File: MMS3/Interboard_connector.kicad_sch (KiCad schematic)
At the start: 1 part, among them J1 86093488324755V1LF

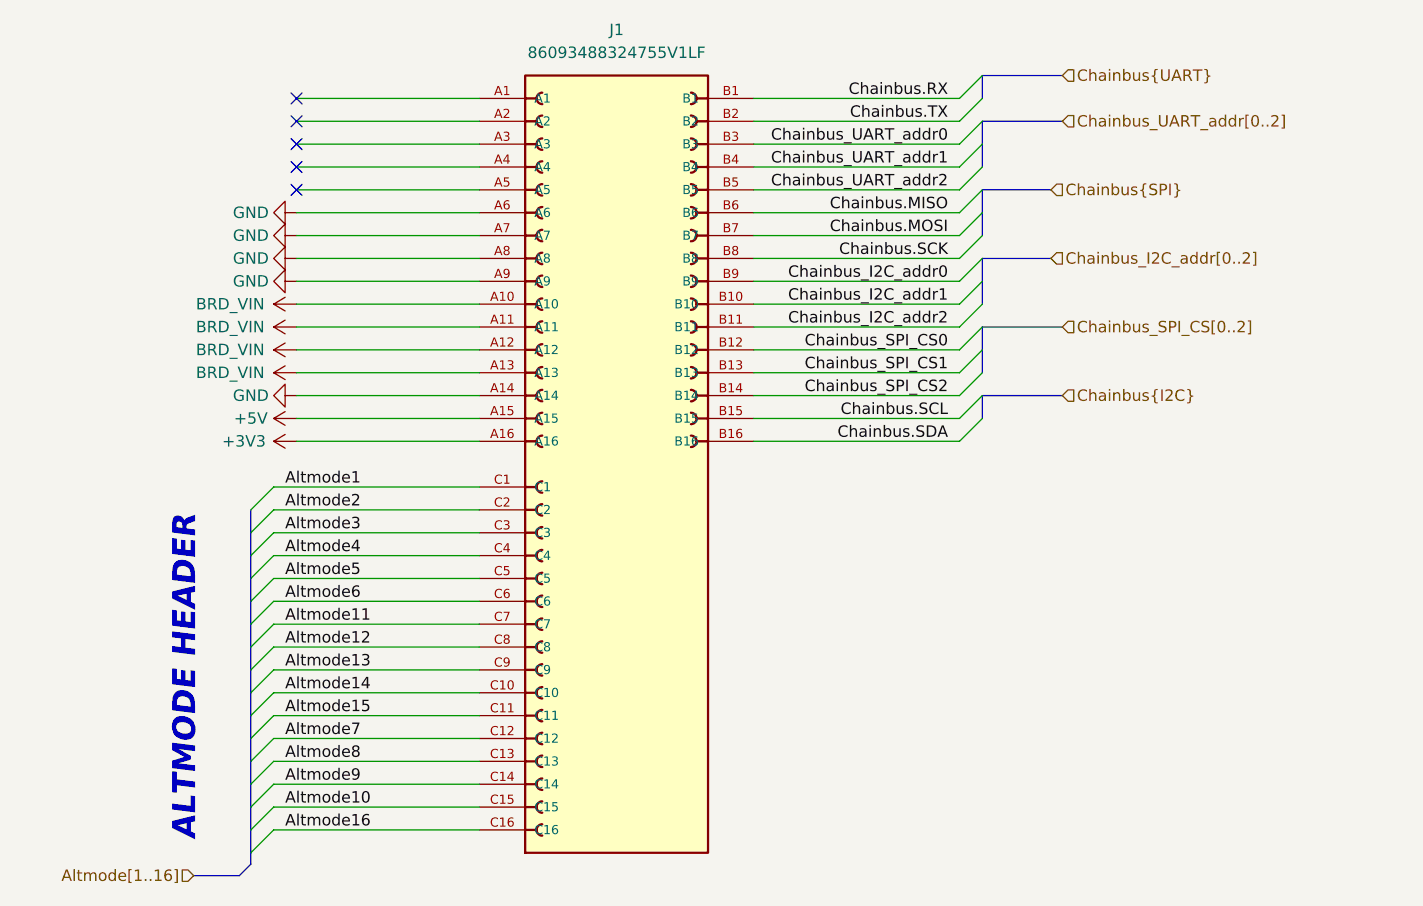
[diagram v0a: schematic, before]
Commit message: schematic + partly layout
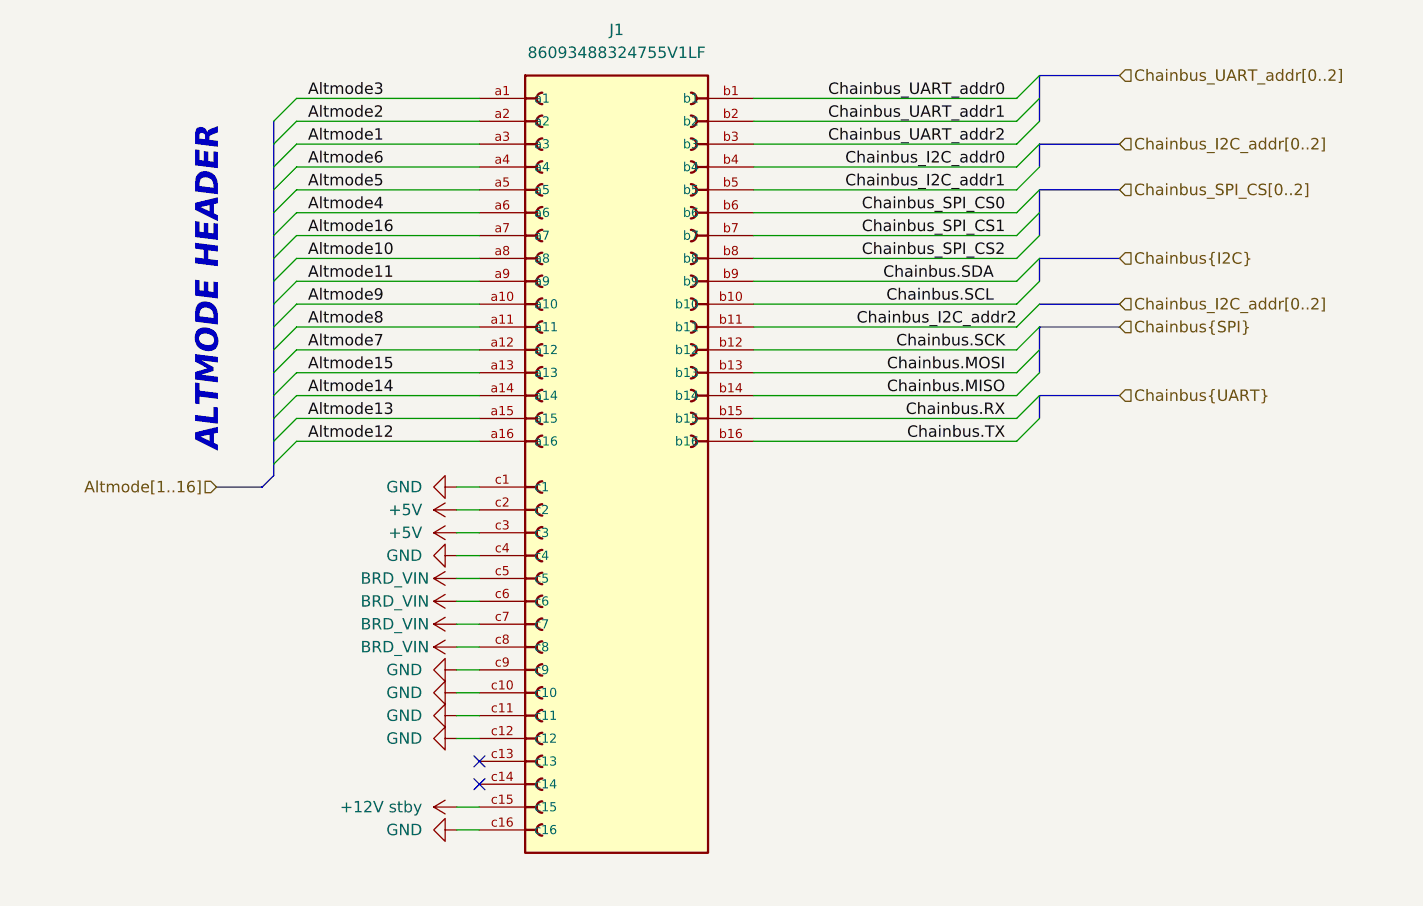
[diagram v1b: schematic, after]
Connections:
- net +5V: now also J1.c2, J1.c3; no longer J1.A15
- net Altmode1: now also J1.a3; no longer J1.C1
- net Altmode10: now also J1.a8; no longer J1.C15
- net Altmode11: now also J1.a9; no longer J1.C7
- net Altmode12: now also J1.a16; no longer J1.C8
- net Altmode13: now also J1.a15; no longer J1.C9
- net Altmode14: now also J1.a14; no longer J1.C10
- net Altmode15: now also J1.a13; no longer J1.C11
- net Altmode16: now also J1.a7; no longer J1.C16
- net Altmode2: now also J1.a2; no longer J1.C2
- net Altmode3: now also J1.a1; no longer J1.C3
- net Altmode4: now also J1.a6; no longer J1.C4
- net Altmode5: now also J1.a5; no longer J1.C5
- net Altmode6: now also J1.a4; no longer J1.C6
- net Altmode7: now also J1.a12; no longer J1.C12
- net Altmode8: now also J1.a11; no longer J1.C13
- net Altmode9: now also J1.a10; no longer J1.C14
- net BRD_VIN: now also J1.c5, J1.c6, J1.c7, J1.c8; no longer J1.A10, J1.A11, J1.A12, J1.A13
- net Chainbus.MISO: now also J1.b14; no longer J1.B6
- net Chainbus.MOSI: now also J1.b13; no longer J1.B7
- net Chainbus.RX: now also J1.b15; no longer J1.B1
- net Chainbus.SCK: now also J1.b12; no longer J1.B8
- net Chainbus.SCL: now also J1.b10; no longer J1.B15
- net Chainbus.SDA: now also J1.b9; no longer J1.B16
- net Chainbus.TX: now also J1.b16; no longer J1.B2
- net Chainbus_I2C_addr0: now also J1.b4; no longer J1.B9
- net Chainbus_I2C_addr1: now also J1.b5; no longer J1.B10
- net Chainbus_I2C_addr2: now also J1.b11; no longer J1.B11
- net Chainbus_SPI_CS0: now also J1.b6; no longer J1.B12
- net Chainbus_SPI_CS1: now also J1.b7; no longer J1.B13
- net Chainbus_SPI_CS2: now also J1.b8; no longer J1.B14
- net Chainbus_UART_addr0: now also J1.b1; no longer J1.B3
- net Chainbus_UART_addr1: now also J1.b2; no longer J1.B4
- net Chainbus_UART_addr2: now also J1.b3; no longer J1.B5
- net GND: now also J1.c1, J1.c10, J1.c11, J1.c12, J1.c16, J1.c4, J1.c9; no longer J1.A14, J1.A6, J1.A7, J1.A8, J1.A9
- removed net +3V3: J1.A16
- new net +12V stby: J1.c15
- no-connect marks 5 -> 2

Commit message: almost done
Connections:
- net Chainbus_I2C_addr0 renamed Chainbus_addr1
- net Chainbus_I2C_addr1 renamed Chainbus_addr2
- net Chainbus_I2C_addr2 renamed Chainbus.CS
- net Chainbus_SPI_CS0 renamed Chainbus_addr5
- net Chainbus_SPI_CS1 renamed Chainbus_addr6
- net Chainbus_SPI_CS2 renamed Chainbus_addr7
- net Chainbus_UART_addr0 renamed Chainbus_addr3
- net Chainbus_UART_addr1 renamed Chainbus_addr4
- net Chainbus_UART_addr2 renamed Chainbus_addr0
